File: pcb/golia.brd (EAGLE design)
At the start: 49.7 x 32 mm, 23 parts, among them IC1 xm64a4u, IC2 LM340MP, X2 EXT

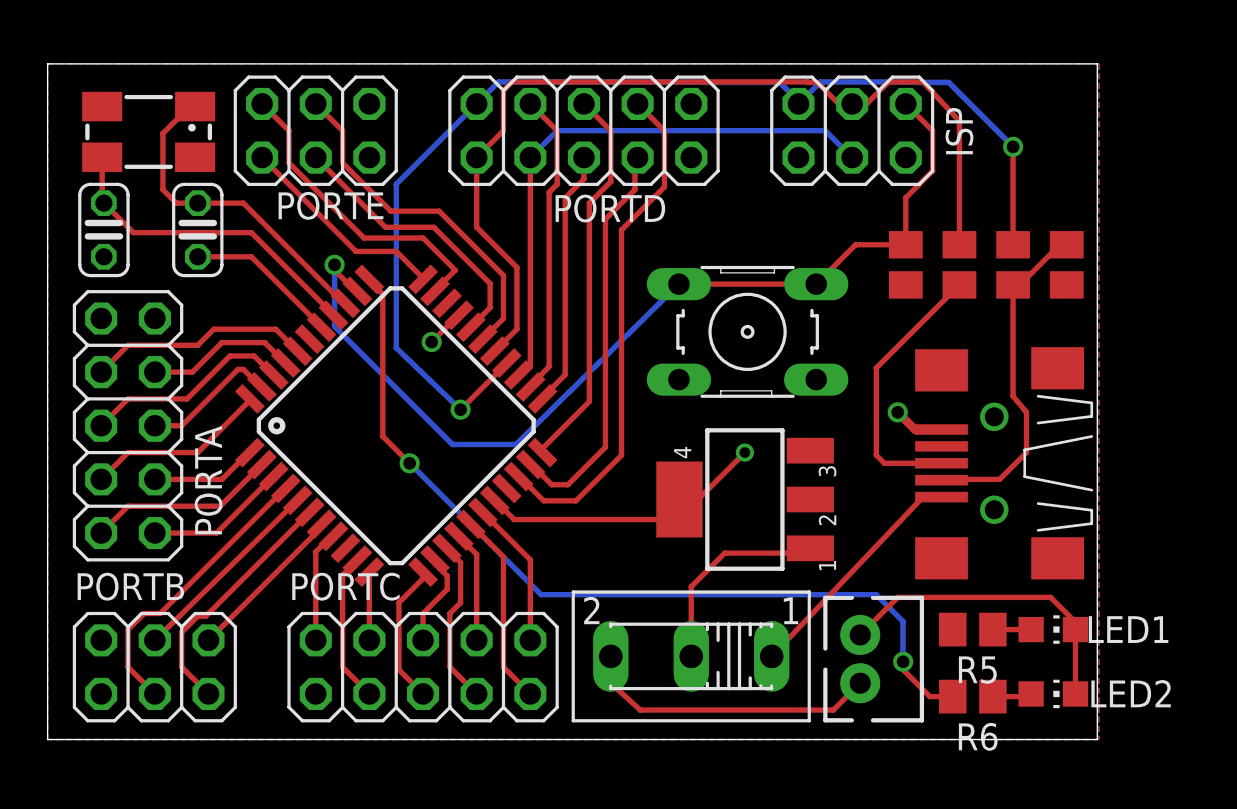
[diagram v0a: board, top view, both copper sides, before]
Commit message: Changed component packages
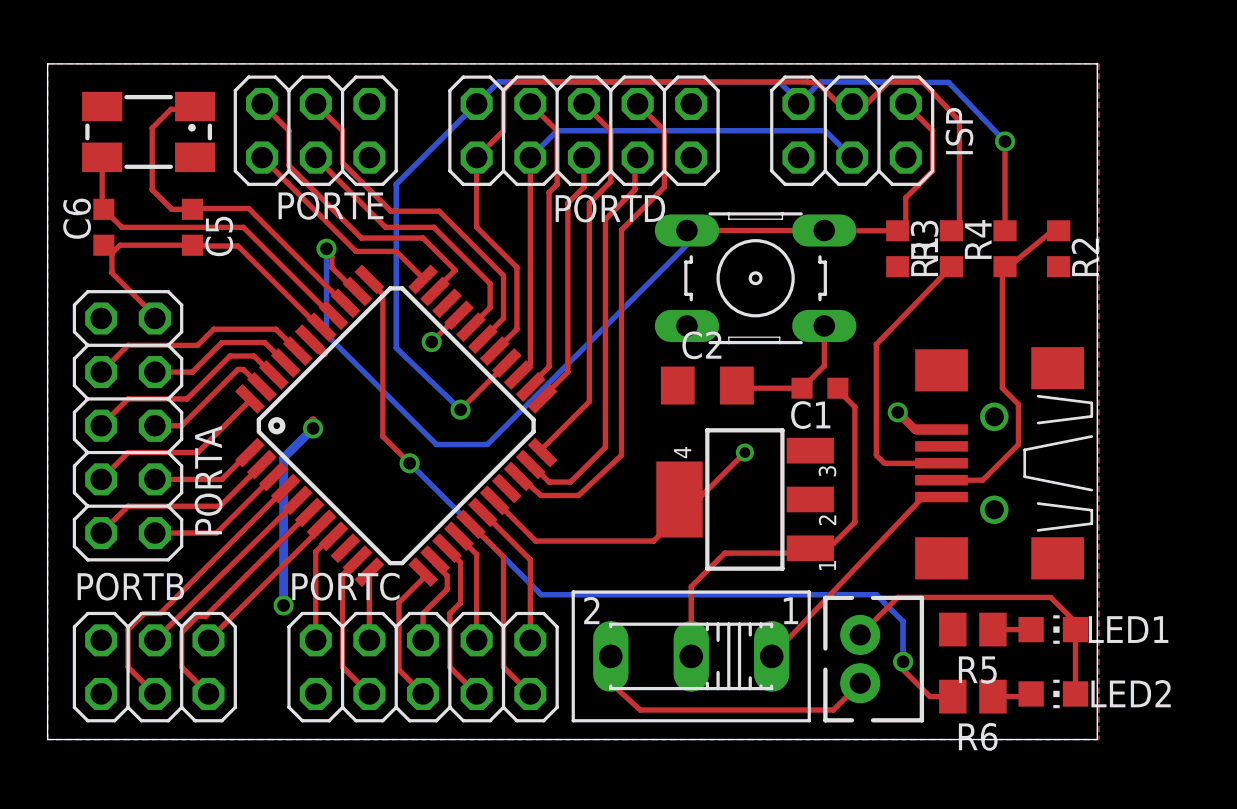
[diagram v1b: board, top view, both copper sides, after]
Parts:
- added C5, C6: 22p, Passives:C0603
- C1: value 22p -> 10u; device resistor:C025-024X044 -> Passives:C0603
- C2: value 22p -> 100u; device resistor:C025-024X044 -> rcl:C1206
- R1: value 10k -> 10K; device resistor:M0805 -> rcl:R0603
- R2: value 1.5k -> 1.5K; device resistor:M0805 -> rcl:R0603
- R3, R4: device resistor:M0805 -> rcl:R0603
- moved C1 30.4 mm to (36.6, 16.6), turned to 180 degrees
- moved C2 29.5 mm to (31.2, 16.8), turned to 0 degrees
- moved S1 2.57 mm to (33.5, 21.8)
- moved R1 0.85 mm to (40.3, 23.2)
- moved R2 0.85 mm to (47.9, 23.2)
- moved R3 0.85 mm to (42.8, 23.2)
- moved R4 0.85 mm to (45.3, 23.2)
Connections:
- net +3V3: now also C2.1
- net GND: now also C1.2, C2.2, C5.2, C6.1; no longer C1.1, C2.1
- net N$23: now also C5.1; no longer C1.2
- net N$24: now also C6.2; no longer C2.2
- net N$5: now also C1.1
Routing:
- net GND: track 45.7 -> 62.0 mm
- net +3V3: track 0.00 -> 10.6 mm, vias 0 -> 2
- net N$5: track 9.69 -> 19.0 mm
- net !RESET: track 45.7 -> 47.8 mm
- net N$23: track 15.6 -> 16.8 mm
- net PD6: track 53.1 -> 52.3 mm
- net N$4: track 12.9 -> 13.6 mm
- net N$3: track 16.0 -> 16.6 mm

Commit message: Changed layout of board, USB now central
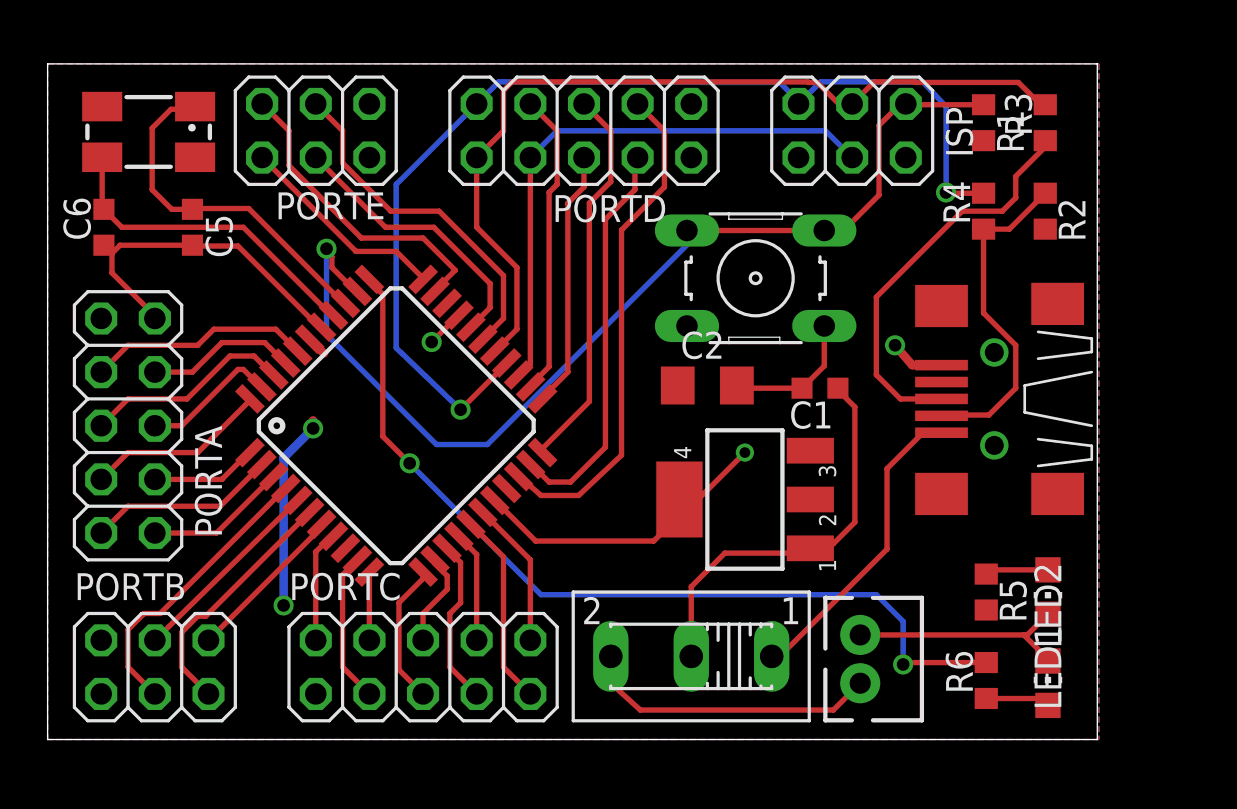
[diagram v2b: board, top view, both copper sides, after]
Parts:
- R5, R6: device resistor:M0805 -> rcl:R0603
- moved R3 7.44 mm to (47.2, 29.2)
- moved R1 7.22 mm to (44.3, 29.2)
- moved X1 3.05 mm to (44.8, 16.1)
- moved R4 2.05 mm to (44.3, 25.0)
- moved R5 1.89 mm to (44.5, 6.99), turned to 270 degrees
- moved R2 1.89 mm to (47.2, 25.0)
- moved LED1 1.80 mm to (47.4, 6.99), turned to 180 degrees
- moved R6 0.99 mm to (44.5, 2.79), turned to 90 degrees
- moved LED2 0.57 mm to (47.4, 2.67), turned to 0 degrees
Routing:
- net N$4: track 13.6 -> 19.1 mm
- net GND: track 62.0 -> 58.3 mm
- net N$2: track 11.3 -> 14.7 mm
- net PD6: track 52.3 -> 50.4 mm
- net PD7: track 42.9 -> 41.2 mm
- net !RESET: track 47.8 -> 49.1 mm
- net N$8: track 1.81 -> 3.00 mm
- net N$9: track 1.94 -> 3.06 mm
- net LED: track 41.1 -> 42.0 mm
- net N$3: track 16.6 -> 15.8 mm

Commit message: Added Silkscreen for ports
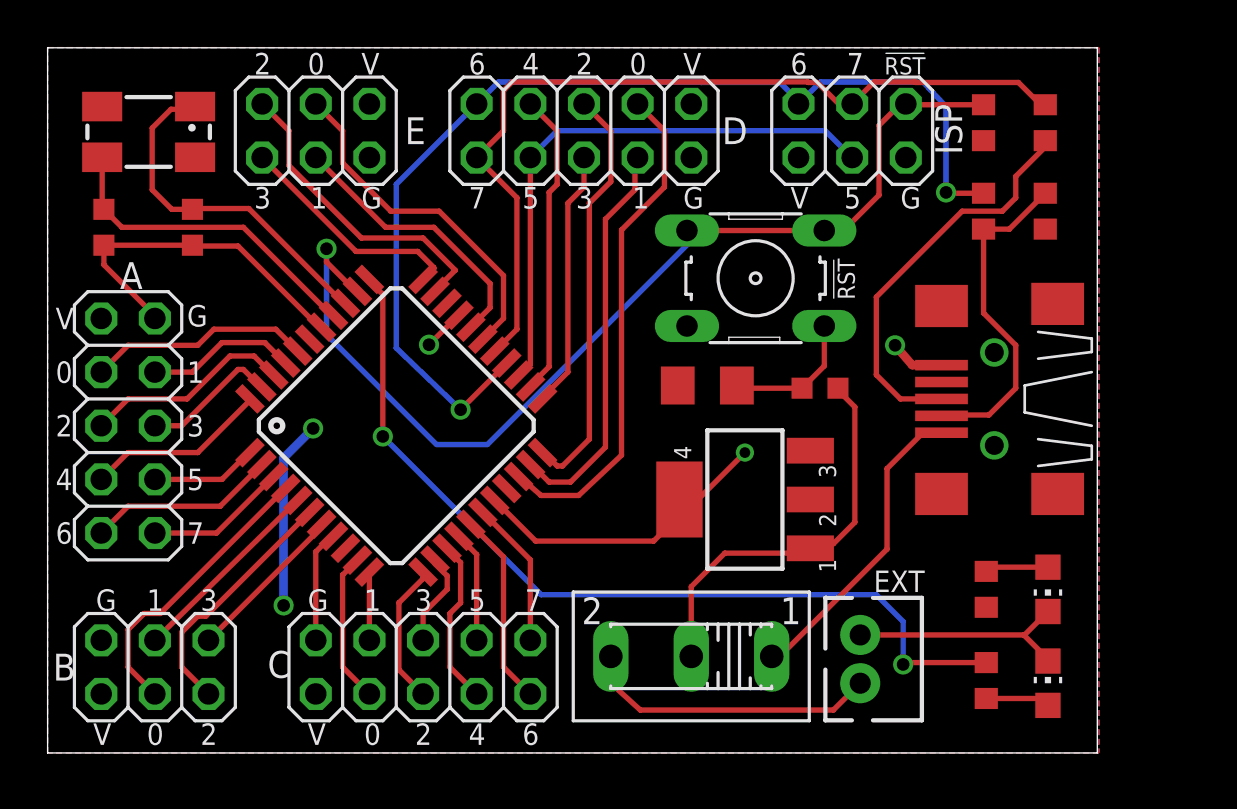
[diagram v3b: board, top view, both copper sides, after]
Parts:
- LED1: value Power -> PWR
- moved LED1 0.13 mm to (47.4, 7.11)
- moved R5 0.13 mm to (44.5, 7.11)
- renumbered PORTA to A, PORTB to B, PORTC to C, PORTD to D, PORTE to E
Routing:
- net +3V3: track 10.6 -> 8.96 mm
- net PD2: track 18.4 -> 19.8 mm
- net PE3: track 10.0 -> 11.1 mm
- net GND: track 58.3 -> 59.0 mm
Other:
- board size 49.7 x 32 mm -> 49.7 x 33.4 mm
- board text added: "!RST"
- board text added: "0"
- board text added: "1"
- board text added: "2"
- board text added: "3"
- board text added: "4"
- board text added: "5"
- board text added: "6"
- board text added: "7"
- board text added: "A"
- board text added: "B"
- board text added: "C"
- board text added: "D"
- board text added: "E"
- board text added: "EXT"
- board text added: "G"
- board text added: "ISP"
- board text added: "V"

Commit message: * Swapped out the power switch, regulator, and USB connector with those available free from the uni * Fattened up some of the power supply traces.
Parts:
- removed IC2: LM340MP, linear:SOT223
- removed S2: (no value), switch:255SB
- removed X1: (no value), con-usb-3:USB-MB-S
- added S3: SPDTEG-1218, Switches:EG-1218
- added U$1: USB-MINIB-PTH, Connectors:USB-MINIB-PTH
- added U1: MCP1825S-3302E/DB, mcp1825:SOT230P700X180-4N
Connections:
- net +3V3: now also U1.3; no longer IC2.3
- net GND: now also U$1.GND, U$1.P$6, U$1.P$7, U1.2, U1.4; no longer IC2.4, X1.GND
- net N$1: now also S3.1; no longer S2.3
- net N$2: now also S3.3, U$1.VBUS; no longer S2.1, X1.VBUS
- net N$3: now also U$1.D-; no longer X1.D-
- net N$4: now also U$1.D+; no longer X1.D+
- net N$5: now also S3.2, U1.1; no longer IC2.1, S2.2
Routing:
- net GND: track 59.0 -> 56.7 mm, vias 3 -> 2
- net N$4: track 19.1 -> 17.6 mm
- net N$1: track 14.1 -> 12.8 mm

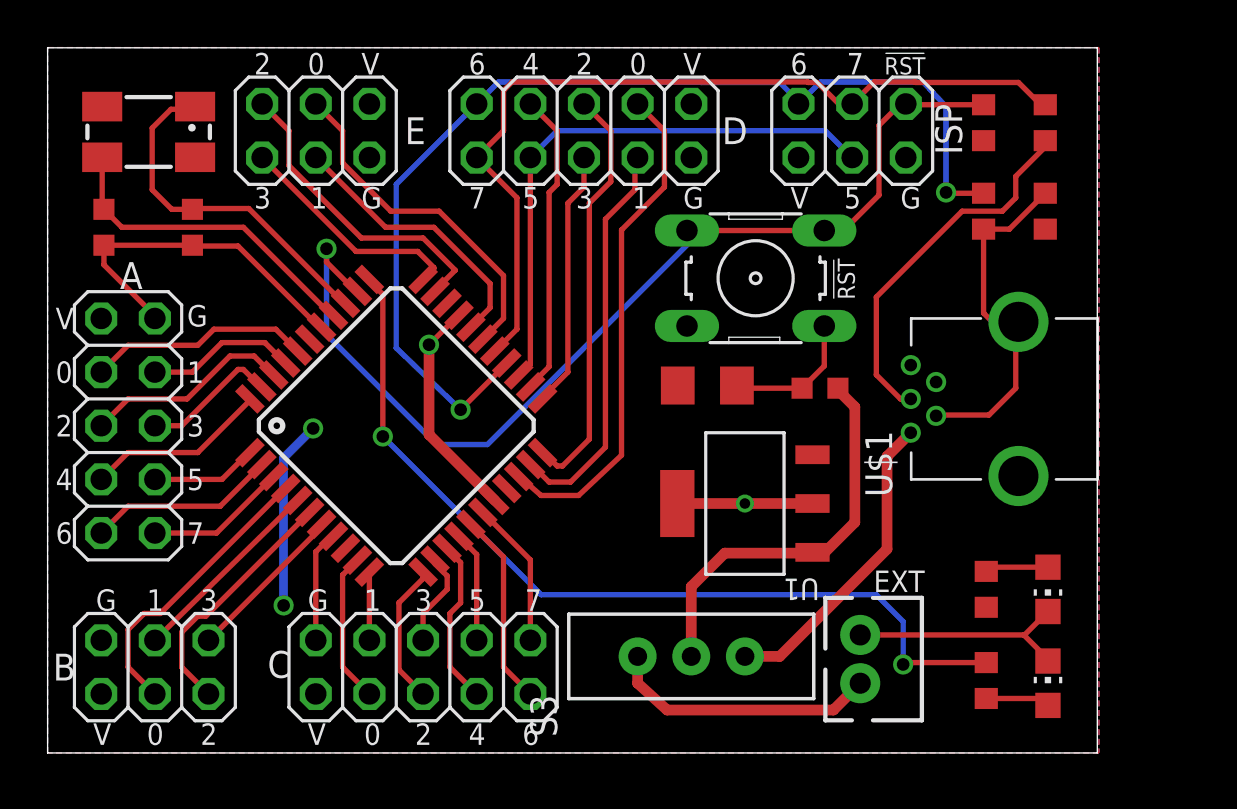
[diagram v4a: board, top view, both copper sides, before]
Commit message: Added names to silk screen increased board size to fit port silks
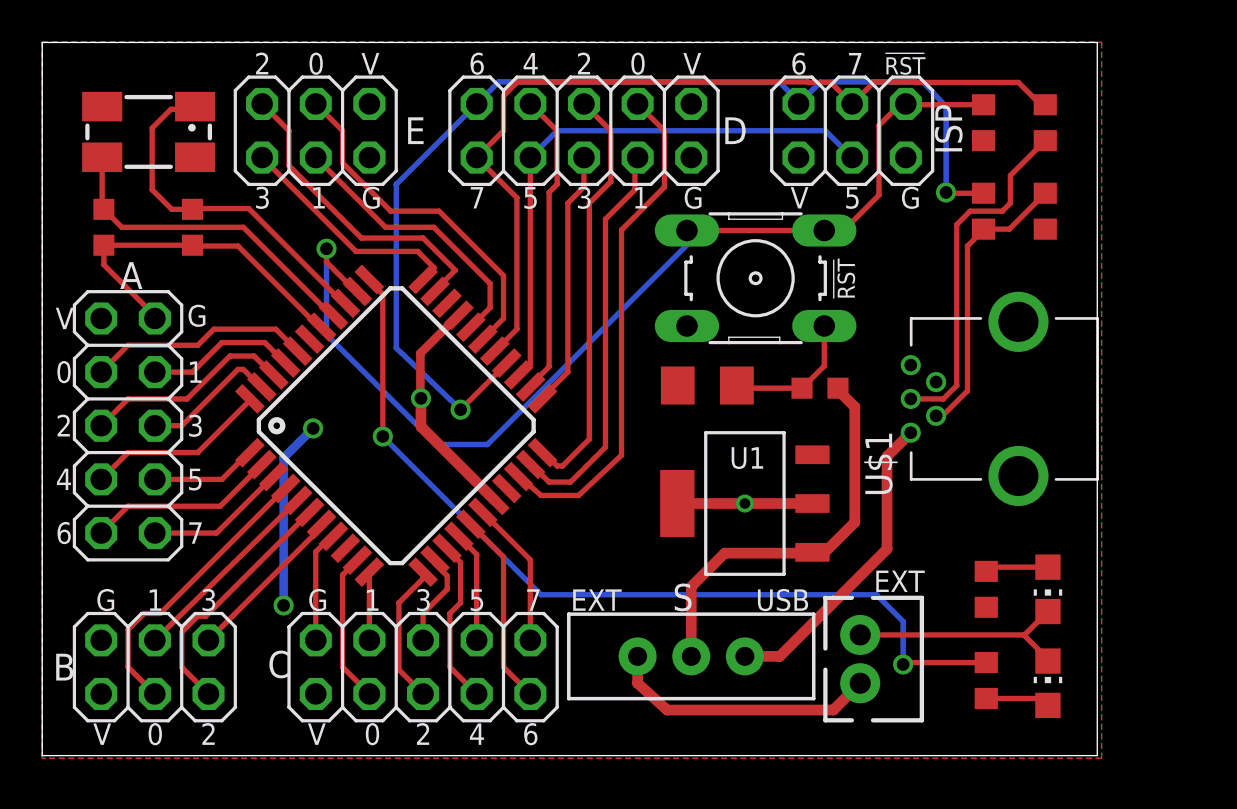
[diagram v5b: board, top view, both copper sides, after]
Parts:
- S: value SPDTEG-1218 -> 3
- renumbered S3 to S
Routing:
- net N$3: track 16.1 -> 13.6 mm
- net N$4: track 17.6 -> 16.7 mm
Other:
- board size 49.7 x 33.4 mm -> 50 x 33.8 mm
- board text added: "GOLIA"
- board text added: "Rhys Thomas Tom Darlison George Brown Harry Beadle"
- board text added: "USB"

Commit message: Changes to LEDs
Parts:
- removed C5, C6: 22p, Passives:C0603
- removed Q1: (no value), adafruit:CTS406
- added LED3: LED1, led:CHIP-LED0805
- added R7: 330, rcl:R0603
- LED2: value LED -> LED2
- moved LED1 50.4 mm to (2.67, 30.5), turned to 90 degrees
- moved LED2 49.7 mm to (2.67, 24.4), turned to 90 degrees
- moved R5 44.5 mm to (6.60, 30.5), turned to 0 degrees
- moved R6 43.6 mm to (6.60, 24.4), turned to 0 degrees
- renumbered U$1 to USB
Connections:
- removed net LED: IC1.34, R6.2
- removed net N$23: C5.1, IC1.36, Q1.1
- removed net N$24: C6.2, IC1.37, Q1.3
- new net LED1: IC1.37, R6.2
- new net LED2: IC1.36, R7.2
- new net N$10: LED3.A, R7.1
- net GND: now also LED3.C; no longer C5.2, C6.1
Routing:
- net LED: track 42.0 -> 0.00 mm, vias 2 -> 0
- net N$23: track 16.8 -> 0.00 mm
- net N$24: track 15.4 -> 0.00 mm
- net LED2: track 0.00 -> 9.51 mm
- net LED1: track 0.00 -> 7.88 mm
- net GND: track 56.9 -> 49.8 mm
- net !RESET: track 49.1 -> 43.8 mm
- net N$10: track 0.00 -> 2.04 mm
- net N$9: track 3.06 -> 2.04 mm
- net N$8: track 2.98 -> 2.04 mm
